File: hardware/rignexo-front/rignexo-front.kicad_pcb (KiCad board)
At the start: 2 copper layers, 45 x 19.5 mm, 4 parts

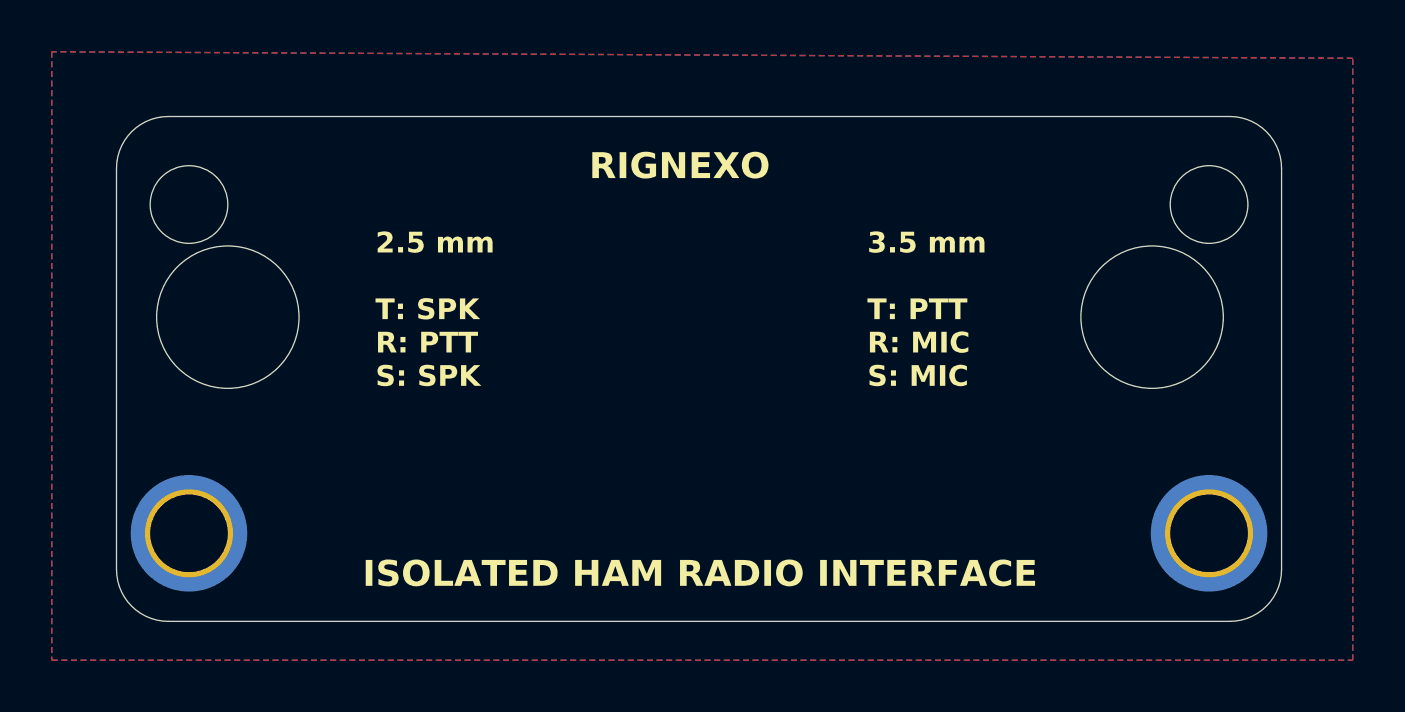
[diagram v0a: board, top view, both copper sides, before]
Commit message: Adjust the front-panel board edge to improve electrical contact with the metal enclosure.
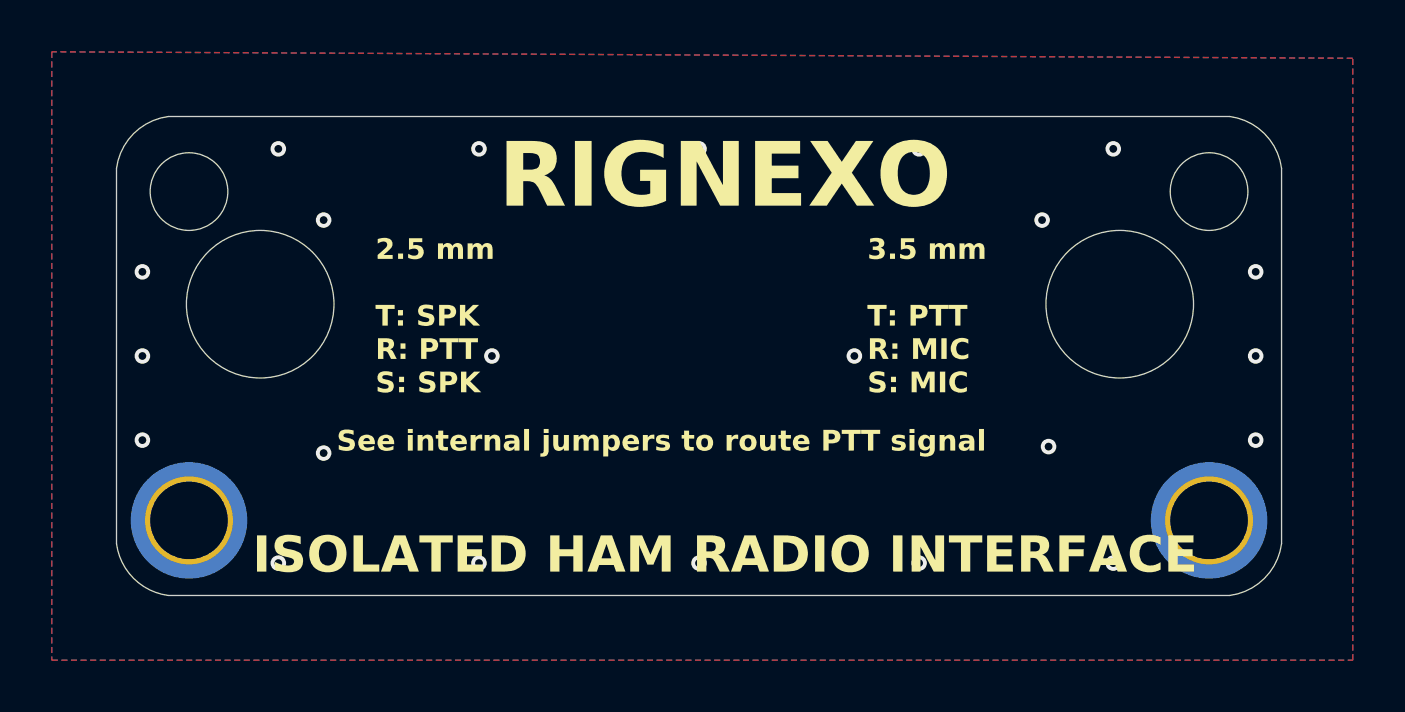
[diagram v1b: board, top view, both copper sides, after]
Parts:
- moved H1 0.50 mm to (102.8, 102.9)
- moved H2 0.50 mm to (142.2, 102.9)
- moved H3 0.50 mm to (102.8, 115.6)
- moved H4 0.50 mm to (142.2, 115.6)
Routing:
- net GND: vias 0 -> 22
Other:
- board size 45 x 19.5 mm -> 45 x 19 mm
- board text added: "See internal jumpers to route PTT signal"
